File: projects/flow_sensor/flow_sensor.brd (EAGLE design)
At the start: 39.4 x 49.5 mm, 92 parts, among them J1 1X07_CONNECTOR, J2 1X03_CONNECTOR, U1 LTC1517-5, U2 XC6805, U3 MAX1726, U4 ADT7320, U5 AD8222, U6 LM321, U7 TRF7970A, U8 RM25C256C, U9 F552X---PN80, Y1 13.56MHz, Y2 32.768kHz, Y3 4MHz

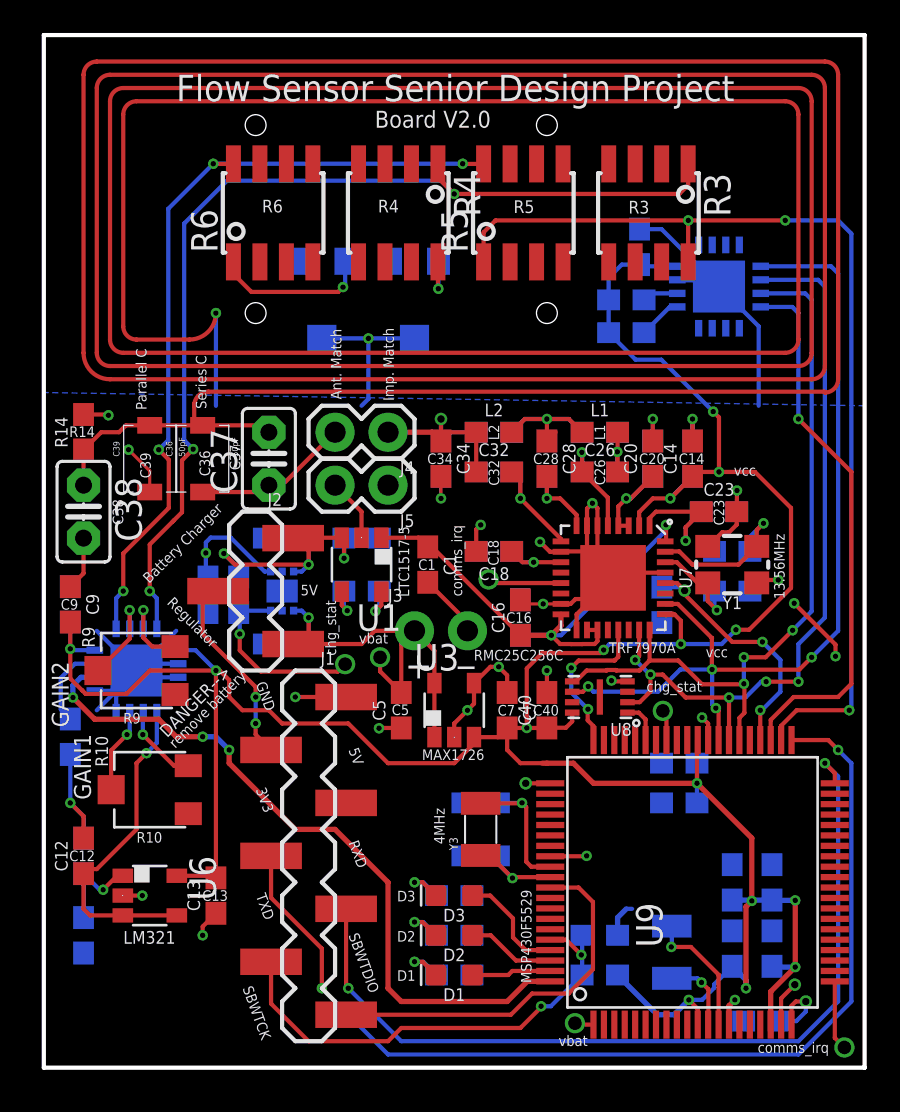
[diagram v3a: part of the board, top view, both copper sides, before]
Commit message: Rewired SBW interface pins, LEDs, and Vbat bridge wire
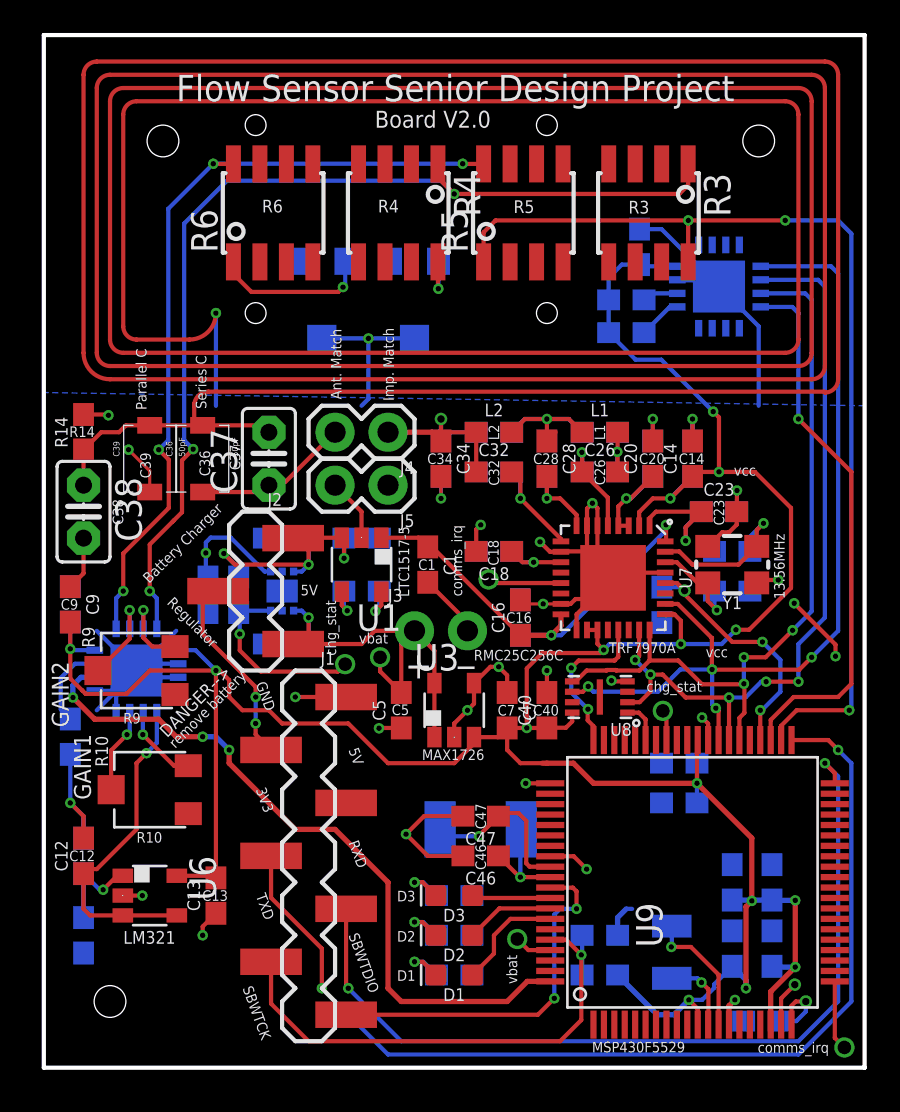
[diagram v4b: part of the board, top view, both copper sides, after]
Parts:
- Y3: value 4MHz -> 8MHz; device my_library:CRYSTAL-3.2X1.5 -> my_library:CRYSTAL-3.2X2.5
- moved C47 0.63 mm to (21.0, 12.1), flipped to the top, turned to 180 degrees
- flipped C46 to the top, turned to 180 degrees
- flipped Y3 to the bottom, turned to 0 degrees
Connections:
- removed net N$17: D3.A, U9.77
- removed net N$5: D1.A, U9.79
- removed net N$7: D2.A, U9.78
- new net D1: D1.A, U9.74
- new net D2: D2.A, U9.73
- new net D3: D3.A, U9.72
- net N$28: now also Y3.2; no longer Y3.P$2
- net N$30: now also Y3.1; no longer Y3.P$1
- net VBAT: now also U9.77; no longer U9.1
- net VCC: now also U7.18, U7.19
- net VIN: no longer U7.18, U7.19
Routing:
- net GND: track 494.3 -> 500.8 mm, vias 28 -> 29
- net D1: track 0.00 -> 5.36 mm
- net N$17: track 5.35 -> 0.00 mm
- net D2: track 0.00 -> 4.26 mm
- net N$7: track 4.23 -> 0.00 mm
- net N$5: track 3.81 -> 0.00 mm
- net D3: track 0.00 -> 3.78 mm
- net VIN: track 25.2 -> 21.7 mm
- net SBWTDIO: track 22.8 -> 24.9 mm, vias 2 -> 1
- net VCC: track 144.9 -> 146.4 mm
- net N$28: track 7.27 -> 8.17 mm
- net VBAT: track 21.4 -> 22.3 mm
- net SBWTCK: track 18.3 -> 17.7 mm, vias 0 -> 2
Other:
- board text added: "8MHz"
- board text removed: "4MHz"

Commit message: Board 2 complete
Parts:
- C1, C10, C13, C14, C15, C16, C17, C18, C19, C2, C20, C21, C22, C23, C24, C25, C26, C27, C28, C29, C3, C30, C31, C32, C33, C34, C35, C4, C40, C42, C44, C45, C46, C47, C49, C5, C50, C6, C7, C8, C9: device SparkFun-Capacitors:0603 -> my_library:0603
- C11, C12: value 3uF -> 3.3uF; device SparkFun-Capacitors:0603 -> my_library:0603
- C41, C43, C48: value 1.0uF -> 1uF; device SparkFun-Capacitors:0603 -> my_library:0603
- L1, L2: device SparkFun-Coils:0603 -> my_library:0603
- R1, R11, R12, R13, R14, R15, R16, R17, R18, R2, R7, R8: device SparkFun-Resistors:0603 -> my_library:0603
- R10, R19, R20, R9: device my_library:PVG3G_TRIM_POT -> my_library:ST-32ETA
- R3, R4, R5, R6: device my_library:SOIC-8 -> my_library:SOIC-8-NOCREAM
- moved R19 6.48 mm to (19.7, 35.6), turned to 270 degrees
- moved R20 4.02 mm to (14.0, 35.6), turned to 90 degrees
- moved R9 0.90 mm to (5.08, 19.7), turned to 270 degrees
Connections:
- removed net N$33: R19.1, R6.1
- removed net N$35: R20.1, R4.8
- new net N$5: R19.1, R4.8
- new net N$7: R20.1, R6.1
- net GND: now also Y1.2, Y1.4
- net N$22: now also R9.1; no longer R9.2
- net N$27: now also R9.2; no longer R9.1
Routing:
- net N$33: track 7.60 -> 0.00 mm, vias 1 -> 0
- net N$7: track 0.00 -> 6.74 mm, vias 0 -> 1
- net N$5: track 0.00 -> 5.08 mm, vias 0 -> 1
- net N$35: track 2.61 -> 0.00 mm, vias 1 -> 0
- net N$28: track 8.17 -> 9.64 mm
- net GND: track 500.8 -> 499.6 mm
- net VCC: track 146.4 -> 145.4 mm, vias 15 -> 16
- net N$17: track 3.88 -> 4.55 mm
- net 5V: track 10.9 -> 10.3 mm
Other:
- board text added: "trudy was here"

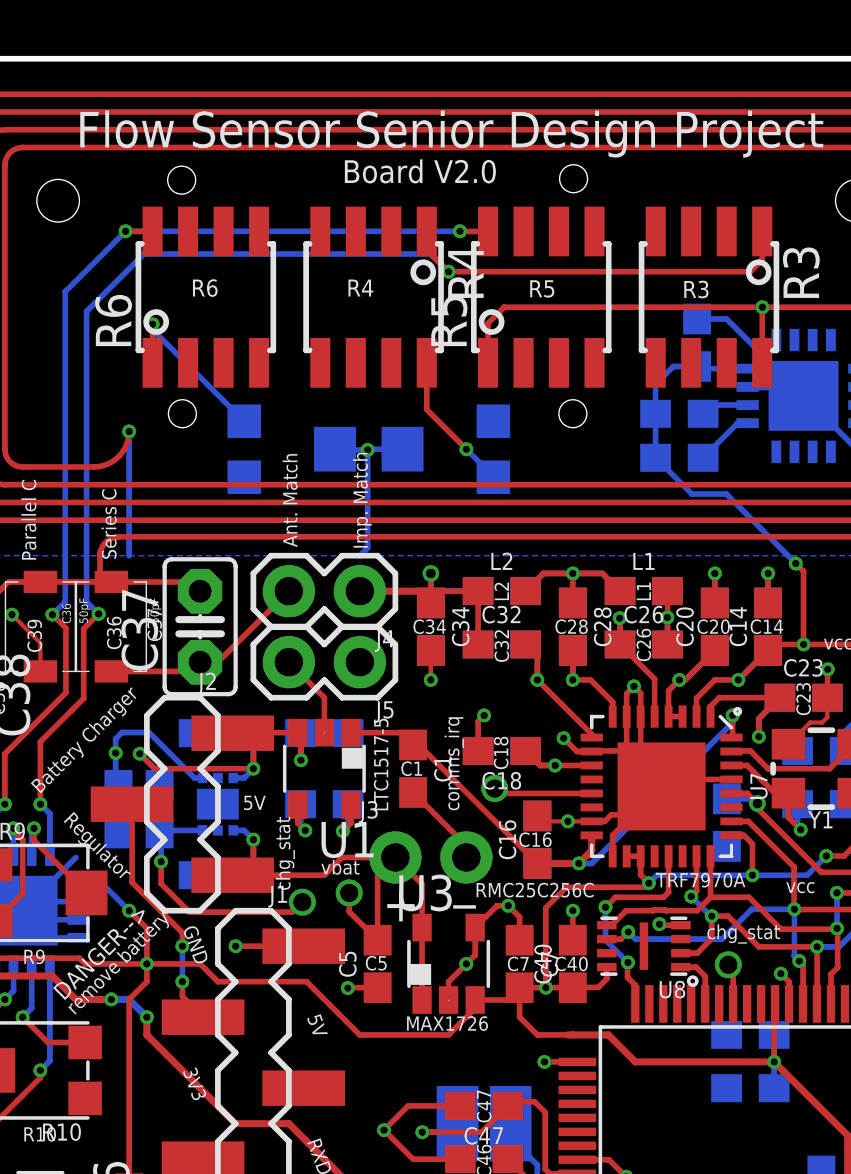
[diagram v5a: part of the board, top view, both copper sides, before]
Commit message: Not important changes to board v2: WP and HOLD on EEPROM connected, shifted top 2 channel tiedown holes 1 mil right
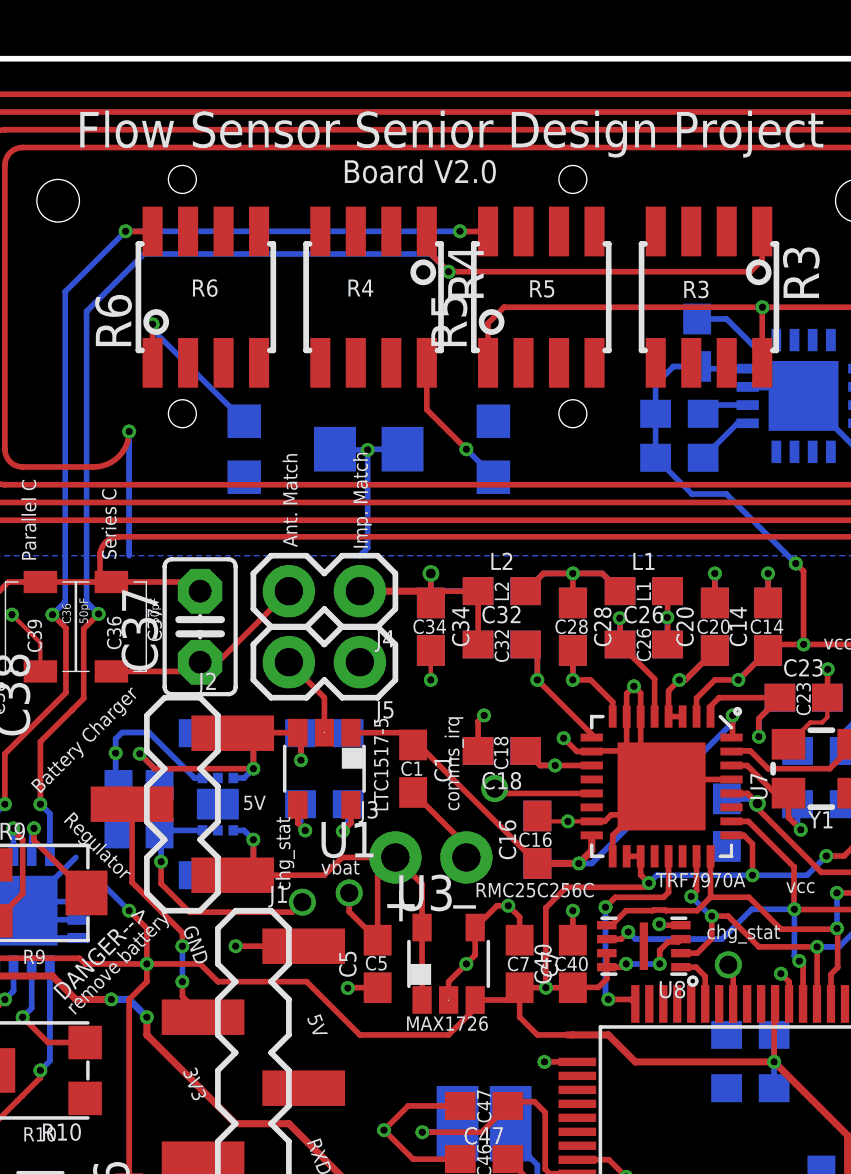
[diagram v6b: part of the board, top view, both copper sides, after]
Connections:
- net VCC: now also U8.3, U8.7
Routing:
- net VCC: track 145.4 -> 149.2 mm, vias 16 -> 18
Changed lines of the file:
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@@
 <?xml version="1.0" encoding="utf-8"?>
 <!DOCTYPE eagle SYSTEM "eagle.dtd">
-<eagle version="8.6.1">
+<eagle version="8.4.3">
 <drawing>
 <settings>
@@
 <grid distance="25" unitdist="mil" unit="mil" style="lines" multiple="2" display="yes" altdistance="1" altunitdist="mil" altunit="mil"/>
 <layers>
-<layer number="1" name="Top" color="4" fill="1" visible="no" active="yes"/>
+<layer number="1" name="Top" color="4" fill="1" visible="yes" active="yes"/>
 <layer number="16" name="Bottom" color="1" fill="1" visible="yes" active="yes"/>
 <layer number="17" name="Pads" color="2" fill="1" visible="yes" active="yes"/>
@@
 <layer number="19" name="Unrouted" color="6" fill="1" visible="yes" active="yes"/>
 <layer number="20" name="Dimension" color="24" fill="1" visible="yes" active="yes"/>
-<layer number="21" name="tPlace" color="7" fill="1" visible="no" active="yes"/>
+<layer number="21" name="tPlace" color="7" fill="1" visible="yes" active="yes"/>
 <layer number="22" name="bPlace" color="7" fill="1" visible="yes" active="yes"/>
-<layer number="23" name="tOrigins" color="15" fill="1" visible="no" active="yes"/>
-<layer number="24" name="bOrigins" color="15" fill="1" visible="no" active="yes"/>
-<layer number="25" name="tNames" color="7" fill="1" visible="no" active="yes"/>
-<layer number="26" name="bNames" color="7" fill="1" visible="no" active="yes"/>
-<layer number="27" name="tValues" color="7" fill="1" visible="no" active="yes"/>
-<layer number="28" name="bValues" color="7" fill="1" visible="no" active="yes"/>
+<layer number="23" name="tOrigins" color="15" fill="1" visible="yes" active="yes"/>
+<layer number="24" name="bOrigins" color="15" fill="1" visible="yes" active="yes"/>
+<layer number="25" name="tNames" color="7" fill="1" visible="yes" active="yes"/>
+<layer number="26" name="bNames" color="7" fill="1" visible="yes" active="yes"/>
+<layer number="27" name="tValues" color="7" fill="1" visible="yes" active="yes"/>
+<layer number="28" name="bValues" color="7" fill="1" visible="yes" active="yes"/>
 <layer number="29" name="tStop" color="7" fill="3" visible="no" active="yes"/>
 <layer number="30" name="bStop" color="7" fill="6" visible="no" active="yes"/>
@@
 <layer number="37" name="tTest" color="7" fill="1" visible="no" active="yes"/>
 <layer number="38" name="bTest" color="7" fill="1" visible="no" active="yes"/>
-<layer number="39" name="tKeepout" color="4" fill="11" visible="no" active="yes"/>
-<layer number="40" name="bKeepout" color="1" fill="11" visible="no" active="yes"/>
-<layer number="41" name="tRestrict" color="4" fill="10" visible="no" active="yes"/>
-<layer number="42" name="bRestrict" color="1" fill="10" visible="no" active="yes"/>
+<layer number="39" name="tKeepout" color="4" fill="11" visible="yes" active="yes"/>
+<layer number="40" name="bKeepout" color="1" fill="11" visible="yes" active="yes"/>
+<layer number="41" name="tRestrict" color="4" fill="10" visible="yes" active="yes"/>
+<layer number="42" name="bRestrict" color="1" fill="10" visible="yes" active="yes"/>
 <layer number="43" name="vRestrict" color="2" fill="10" visible="no" active="yes"/>
-<layer number="44" name="Drills" color="7" fill="1" visible="no" active="yes"/>
-<layer number="45" name="Holes" color="7" fill="1" visible="no" active="yes"/>
+<layer number="44" name="Drills" color="7" fill="1" visible="yes" active="yes"/>
+<layer number="45" name="Holes" color="7" fill="1" visible="yes" active="yes"/>
 <layer number="46" name="Milling" color="3" fill="1" visible="no" active="yes"/>
 <layer number="47" name="Measures" color="7" fill="1" visible="no" active="yes"/>
@@
 <layer number="49" name="Reference" color="7" fill="1" visible="no" active="yes"/>
 <layer number="50" name="dxf" color="7" fill="1" visible="no" active="no"/>
-<layer number="51" name="tDocu" color="7" fill="1" visible="no" active="yes"/>
+<layer number="51" name="tDocu" color="7" fill="1" visible="yes" active="yes"/>
 <layer number="52" name="bDocu" color="7" fill="1" visible="yes" active="yes"/>
 <layer number="53" name="tGND_GNDA" color="7" fill="9" visible="no" active="no"/>
@@
 <text x="6.2992" y="15.2908" size="0.508" layer="21" rot="R45">remove battery</text>
 <hole x="10.16" y="36.83" drill="1"/>
-<hole x="10.1346" y="45.1866" drill="1"/>
+<hole x="10.16" y="45.212" drill="1"/>
 <hole x="24.13" y="36.83" drill="1"/>
-<hole x="24.1554" y="45.2374" drill="1"/>
+<hole x="24.13" y="45.212" drill="1"/>
 <text x="3.81" y="5.9436" size="0.6096" layer="21">LM321</text>
 <text x="1.2192" y="9.906" size="0.508" layer="21">C12</text>
@@
 <param name="checkRestrict" value="1"/>
 <param name="checkStop" value="0"/>
-<param name="checkValues" value="0"/>
 <param name="useDiameter" value="13"/>
 <param name="maxErrors" value="50"/>
@@
 <wire x1="1.27" y1="18.9738" x2="1.27" y2="20.0914" width="0.2032" layer="1"/>
 <wire x1="2.8956" y1="17.3482" x2="1.27" y2="18.9738" width="0.2032" layer="1"/>
+<contactref element="U8" pad="7"/>
+<contactref element="U8" pad="3"/>
+<wire x1="25.345" y1="17.03" x2="25.345" y2="17.53" width="0.2032" layer="1"/>
+<wire x1="27.995" y1="18.03" x2="27.899" y2="17.934" width="0.2032" layer="1"/>
+<wire x1="27.899" y1="17.934" x2="27.5397875" y2="17.934" width="0.2032" layer="1"/>
+<wire x1="27.5397875" y1="17.934" x2="27.2386" y2="17.6328125" width="0.2032" layer="1"/>
+<wire x1="27.2386" y1="17.6328125" x2="27.2386" y2="17.145" width="0.2032" layer="1"/>
+<via x="27.2386" y="17.145" extent="1-16" drill="0.254"/>
+<wire x1="27.2386" y1="17.145" x2="26.035" y2="17.145" width="0.2032" layer="16"/>
+<via x="26.035" y="17.145" extent="1-16" drill="0.254"/>
+<wire x1="26.035" y1="17.145" x2="25.92" y2="17.03" width="0.2032" layer="1"/>
+<wire x1="25.92" y1="17.03" x2="25.345" y2="17.03" width="0.2032" layer="1"/>
 </signal>
 <signal name="VCHGR">
@@
 <wire x1="27.3775875" y1="19.5289875" x2="25.6503875" y2="19.5289875" width="0.2032" layer="1"/>
 <wire x1="27.555" y1="19.7064" x2="27.3775875" y2="19.5289875" width="0.2032" layer="1"/>
-<wire x1="25.2984" y1="19.177" x2="25.2984" y2="17.9988" width="0.2032" layer="16"/>
-<wire x1="25.2984" y1="17.9988" x2="26.1014" y2="17.1958" width="0.2032" layer="16"/>
-<via x="26.1014" y="17.1958" extent="1-16" drill="0.254"/>
 <contactref element="U9" pad="60"/>
-<wire x1="26.365" y1="15.715" x2="26.365" y2="16.3832" width="0.2032" layer="1"/>
-<wire x1="26.365" y1="16.3832" x2="26.0858" y2="16.6624" width="0.2032" layer="1"/>
-<wire x1="26.0858" y1="16.6624" x2="26.0858" y2="17.1802" width="0.2032" layer="1"/>
-<wire x1="26.0858" y1="17.1802" x2="26.1014" y2="17.1958" width="0.2032" layer="1"/>
+<wire x1="26.365" y1="15.715" x2="26.205" y2="15.875" width="0.2032" layer="1"/>
+<wire x1="26.205" y1="15.875" x2="25.4" y2="15.875" width="0.2032" layer="1"/>
+<via x="25.4" y="15.875" extent="1-16" drill="0.254"/>
+<wire x1="25.4" y1="15.875" x2="25.2984" y2="15.9766" width="0.2032" layer="16"/>
+<wire x1="25.2984" y1="15.9766" x2="25.2984" y2="19.177" width="0.2032" layer="16"/>
 </signal>
 <signal name="N$8">
